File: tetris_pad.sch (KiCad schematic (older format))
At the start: 35 parts, among them P1 video, P2 ICSP, Q1 2N7000, SW1 ~reset, SW2 A, SW3 B, SW4 power, SW5 LEFT, SW6 UP, SW7 DOWN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

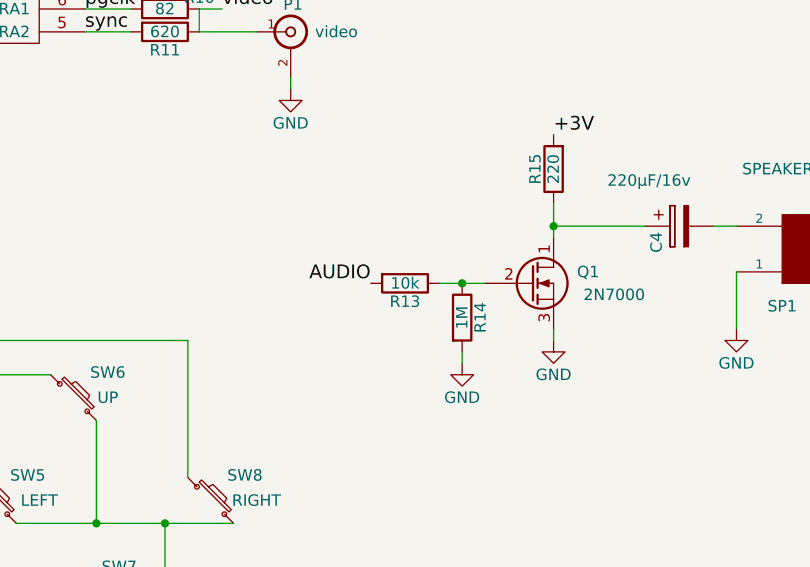
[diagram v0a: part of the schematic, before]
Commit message: schematic rework
renamed project tetris_pad
rework: read_pad, isr, xor_row
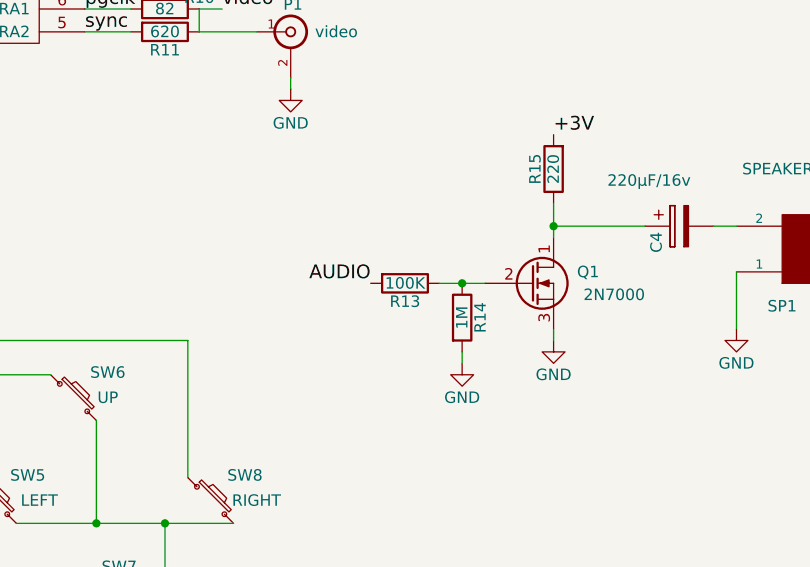
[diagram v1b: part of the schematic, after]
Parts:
- R13: value 10k -> 100K
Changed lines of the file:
@@
 LIBS:valves
 LIBS:Personal_KiCAD
-LIBS:ntsc_test-cache
+LIBS:tetris_pad-cache
 EELAYER 25 0
 EELAYER END
@@
 Wire Wire Line
 	7800 4200 8000 4200
-$Comp
-L R R13
-U 1 1 584C5448
-P 7650 4200
-F 0 "R13" V 7730 4200 50  0000 C CNN
-F 1 "10k" V 7650 4200 50  0000 C CNN
-F 2 "" V 7580 4200 50  0000 C CNN
-F 3 "" H 7650 4200 50  0000 C CNN
-	1    7650 4200
-	0    1    1    0
-$EndComp
 Connection ~ 7900 4200
 Text Label 7500 4200 2    60   ~ 0
@@
 Wire Wire Line
 	4050 4050 3500 4050
+$Comp
+L R R13
+U 1 1 584D7E45
+P 7650 4200
+F 0 "R13" V 7730 4200 50  0000 C CNN
+F 1 "100K" V 7650 4200 50  0000 C CNN
+F 2 "" V 7580 4200 50  0000 C CNN
+F 3 "" H 7650 4200 50  0000 C CNN
+	1    7650 4200
+	0    1    1    0
+$EndComp
 $EndSCHEMATC

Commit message: further optimization
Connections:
- net AUDIO: no longer R3.1, R4.2, R5.1, U1.3 (RA4)
- new net AUDIO/BTN: R3.1, R4.2, R5.1, U1.3 (RA4)
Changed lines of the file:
@@
 AUDIO
 Text Label 5350 3000 2    39   ~ 0
-AUDIO
+AUDIO/BTN
 Wire Wire Line
 	4350 4050 4900 4050

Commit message: finalization
reordering tasks in isr
removed get_next_word from get_nibble, was never called.
actual size: 1031i
My optimization efforts will end here. I can't expect gaining
more than a few instructions.
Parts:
- BT1: value 2xAAA -> CR2450
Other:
- note added: "optional"
- moved on the sheet: C4, Q1, R13, R14, R15, SP1
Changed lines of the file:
@@
 P 4600 2250
 F 0 "BT1" H 4700 2300 50  0000 L CNN
-F 1 "2xAAA" H 4700 2200 50  0000 L CNN
+F 1 "CR2450" H 4700 2200 50  0000 L CNN
 F 2 "" V 4600 2290 50  0000 C CNN
 F 3 "" V 4600 2290 50  0000 C CNN
@@
 L SPEAKER SP1
 U 1 1 58432B86
-P 9400 4050
-F 0 "SP1" H 9300 4300 50  0000 C CNN
-F 1 "SPEAKER 8 ohm" H 9400 3700 50  0000 C CNN
-F 2 "" H 9400 4050 50  0000 C CNN
-F 3 "" H 9400 4050 50  0000 C CNN
-	1    9400 4050
+P 9450 4350
+F 0 "SP1" H 9350 4600 50  0000 C CNN
+F 1 "SPEAKER 8 ohm" H 9450 4000 50  0000 C CNN
+F 2 "" H 9450 4350 50  0000 C CNN
+F 3 "" H 9450 4350 50  0000 C CNN
+	1    9450 4350
 	1    0    0    1
 $EndComp
@@
 L GND #PWR10
 U 1 1 58432BE5
-P 9100 4400
-F 0 "#PWR10" H 9100 4150 50  0001 C CNN
-F 1 "GND" H 9100 4250 50  0000 C CNN
-F 2 "" H 9100 4400 50  0000 C CNN
-F 3 "" H 9100 4400 50  0000 C CNN
-	1    9100 4400
+P 9150 4700
+F 0 "#PWR10" H 9150 4450 50  0001 C CNN
+F 1 "GND" H 9150 4550 50  0000 C CNN
+F 2 "" H 9150 4700 50  0000 C CNN
+F 3 "" H 9150 4700 50  0000 C CNN
+	1    9150 4700
 	-1   0    0    -1
 $EndComp
@@
 L CP C4
 U 1 1 58432C79
-P 8850 3950
-F 0 "C4" H 8875 4050 50  0000 L CNN
-F 1 "220µF/16v" V 8650 3900 50  0000 L CNN
-F 2 "" H 8888 3800 50  0000 C CNN
-F 3 "" H 8850 3950 50  0000 C CNN
-	1    8850 3950
+P 8900 4250
+F 0 "C4" H 8925 4350 50  0000 L CNN
+F 1 "220µF/16v" V 8700 4200 50  0000 L CNN
+F 2 "" H 8938 4100 50  0000 C CNN
+F 3 "" H 8900 4250 50  0000 C CNN
+	1    8900 4250
 	0    -1   1    0
 $EndComp
@@
 	2650 2050 2650 2200
 Wire Wire Line
-	9100 4150 9100 4400
-Wire Wire Line
-	9100 3950 9000 3950
+	9150 4450 9150 4700
+Wire Wire Line
+	9150 4250 9050 4250
 Wire Wire Line
 	4600 5900 5150 5900
@@
 L R R15
 U 1 1 584B92CB
-P 8300 3700
-F 0 "R15" V 8380 3700 50  0000 C CNN
-F 1 "220" V 8300 3700 50  0000 C CNN
-F 2 "" V 8230 3700 50  0000 C CNN
-F 3 "" H 8300 3700 50  0000 C CNN
-	1    8300 3700
+P 8350 4000
+F 0 "R15" V 8430 4000 50  0000 C CNN
+F 1 "220" V 8350 4000 50  0000 C CNN
+F 2 "" V 8280 4000 50  0000 C CNN
+F 3 "" H 8350 4000 50  0000 C CNN
+	1    8350 4000
 	-1   0    0    1
 $EndComp
 Wire Wire Line
-	8300 3950 8700 3950
+	8350 4250 8750 4250
 Wire Wire Line
 	6850 2900 6250 2900
@@
 L Q_NMOS_DGS Q1
 U 1 1 584C4D58
-P 8200 4200
-F 0 "Q1" H 8500 4250 50  0000 R CNN
-F 1 "2N7000" H 8700 4150 50  0000 R CNN
-F 2 "" H 8400 4300 50  0000 C CNN
-F 3 "" H 8200 4200 50  0000 C CNN
-	1    8200 4200
-	1    0    0    -1
-$EndComp
-Text Label 8300 3550 0    60   ~ 0
+P 8250 4500
+F 0 "Q1" H 8550 4550 50  0000 R CNN
+F 1 "2N7000" H 8750 4450 50  0000 R CNN
+F 2 "" H 8450 4600 50  0000 C CNN
+F 3 "" H 8250 4500 50  0000 C CNN
+	1    8250 4500
+	1    0    0    -1
+$EndComp
+Text Label 8350 3850 0    60   ~ 0
 +3V
 Wire Wire Line
-	8300 3850 8300 4000
-Connection ~ 8300 3950
+	8350 4150 8350 4300
+Connection ~ 8350 4250
 $Comp
 L GND #PWR9
 U 1 1 584C5093
-P 8300 4450
-F 0 "#PWR9" H 8300 4200 50  0001 C CNN
-F 1 "GND" H 8300 4300 50  0000 C CNN
-F 2 "" H 8300 4450 50  0000 C CNN
-F 3 "" H 8300 4450 50  0000 C CNN
-	1    8300 4450
+P 8350 4750
+F 0 "#PWR9" H 8350 4500 50  0001 C CNN
+F 1 "GND" H 8350 4600 50  0000 C CNN
+F 2 "" H 8350 4750 50  0000 C CNN
+F 3 "" H 8350 4750 50  0000 C CNN
+	1    8350 4750
 	-1   0    0    -1
 $EndComp
 Wire Wire Line
-	8300 4400 8300 4450
+	8350 4700 8350 4750
 $Comp
 L R R14
 U 1 1 584C5206
-P 7900 4350
-F 0 "R14" V 7980 4350 50  0000 C CNN
-F 1 "1M" V 7900 4350 50  0000 C CNN
-F 2 "" V 7830 4350 50  0000 C CNN
-F 3 "" H 7900 4350 50  0000 C CNN
-	1    7900 4350
+P 7950 4650
+F 0 "R14" V 8030 4650 50  0000 C CNN
+F 1 "1M" V 7950 4650 50  0000 C CNN
+F 2 "" V 7880 4650 50  0000 C CNN
+F 3 "" H 7950 4650 50  0000 C CNN
+	1    7950 4650
 	1    0    0    -1
 $EndComp
@@
 L GND #PWR8
 U 1 1 584C531A
-P 7900 4550
-F 0 "#PWR8" H 7900 4300 50  0001 C CNN
-F 1 "GND" H 7900 4400 50  0000 C CNN
-F 2 "" H 7900 4550 50  0000 C CNN
-F 3 "" H 7900 4550 50  0000 C CNN
-	1    7900 4550
+P 7950 4850
+F 0 "#PWR8" H 7950 4600 50  0001 C CNN
+F 1 "GND" H 7950 4700 50  0000 C CNN
+F 2 "" H 7950 4850 50  0000 C CNN
+F 3 "" H 7950 4850 50  0000 C CNN
+	1    7950 4850
 	-1   0    0    -1
 $EndComp
 Wire Wire Line
-	7900 4500 7900 4550
-Wire Wire Line
-	7800 4200 8000 4200
-Connection ~ 7900 4200
-Text Label 7500 4200 2    60   ~ 0
+	7950 4800 7950 4850
+Wire Wire Line
+	7850 4500 8050 4500
+Connection ~ 7950 4500
+Text Label 7550 4500 2    60   ~ 0
 AUDIO
 Text Label 5350 3000 2    39   ~ 0
@@
 L R R13
 U 1 1 584D7E45
-P 7650 4200
-F 0 "R13" V 7730 4200 50  0000 C CNN
-F 1 "100K" V 7650 4200 50  0000 C CNN
-F 2 "" V 7580 4200 50  0000 C CNN
-F 3 "" H 7650 4200 50  0000 C CNN
-	1    7650 4200
+P 7700 4500
+F 0 "R13" V 7780 4500 50  0000 C CNN
+F 1 "100K" V 7700 4500 50  0000 C CNN
+F 2 "" V 7630 4500 50  0000 C CNN
+F 3 "" H 7700 4500 50  0000 C CNN
+	1    7700 4500
 	0    1    1    0
 $EndComp
+Wire Notes Line
+	7250 3700 7250 5200
+Wire Notes Line
+	7250 5200 9800 5200
+Wire Notes Line
+	9800 5200 9800 3700
+Wire Notes Line
+	9800 3700 7250 3700
+Text Notes 7400 3850 0    60   ~ 0
+optional
 $EndSCHEMATC

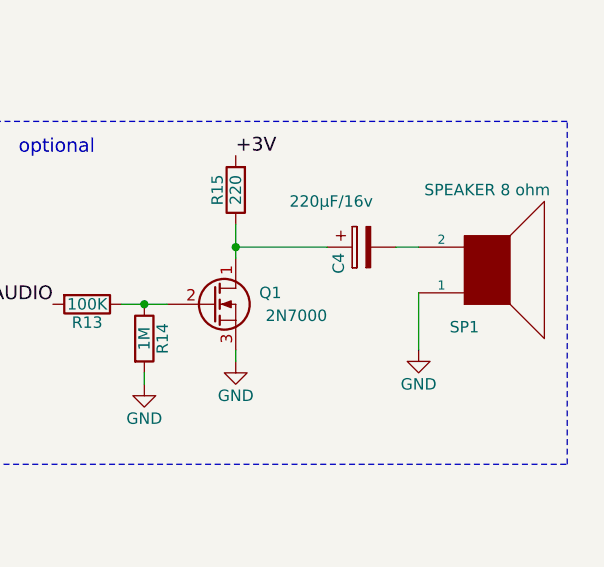
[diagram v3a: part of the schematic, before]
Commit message: modified hardware audio circuit.
audio level to low circuit modified for an output to TV.
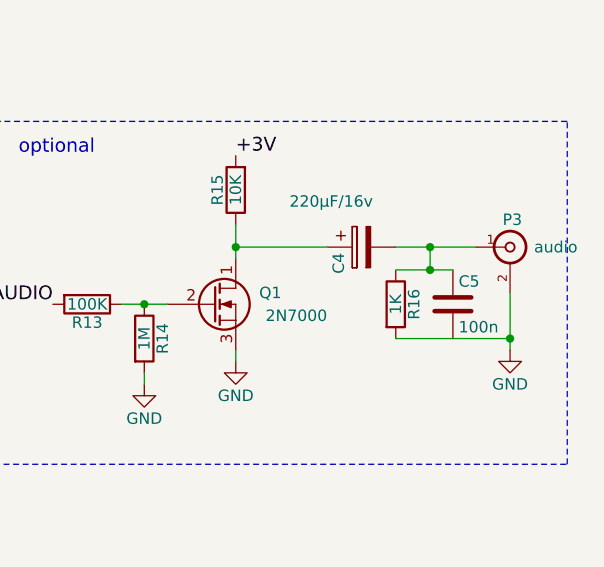
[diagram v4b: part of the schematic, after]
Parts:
- removed SP1: SPEAKER 8 ohm, symbol SPEAKER
- added C5: 100n, symbol C
- added P3: audio, symbol BNC
- added R16: 1K, symbol R
- R15: value 220 -> 10K
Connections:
- net GND: now also P3.2 (Ext), R16.2
- net at C4.2: now also C5.1, P3.1 (In), R16.1
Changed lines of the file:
@@
 Vpp/~rst
-$Comp
-L SPEAKER SP1
-U 1 1 58432B86
-P 9450 4350
-F 0 "SP1" H 9350 4600 50  0000 C CNN
-F 1 "SPEAKER 8 ohm" H 9450 4000 50  0000 C CNN
-F 2 "" H 9450 4350 50  0000 C CNN
-F 3 "" H 9450 4350 50  0000 C CNN
-	1    9450 4350
-	1    0    0    1
-$EndComp
 $Comp
 L GND #PWR10
 U 1 1 58432BE5
-P 9150 4700
-F 0 "#PWR10" H 9150 4450 50  0001 C CNN
-F 1 "GND" H 9150 4550 50  0000 C CNN
-F 2 "" H 9150 4700 50  0000 C CNN
-F 3 "" H 9150 4700 50  0000 C CNN
-	1    9150 4700
+P 9550 4700
+F 0 "#PWR10" H 9550 4450 50  0001 C CNN
+F 1 "GND" H 9550 4550 50  0000 C CNN
+F 2 "" H 9550 4700 50  0000 C CNN
+F 3 "" H 9550 4700 50  0000 C CNN
+	1    9550 4700
 	-1   0    0    -1
 $EndComp
@@
 	2650 2050 2650 2200
 Wire Wire Line
-	9150 4450 9150 4700
-Wire Wire Line
-	9150 4250 9050 4250
+	9550 4450 9550 4700
+Wire Wire Line
+	9050 4250 9400 4250
 Wire Wire Line
 	4600 5900 5150 5900
@@
 P 8350 4000
 F 0 "R15" V 8430 4000 50  0000 C CNN
-F 1 "220" V 8350 4000 50  0000 C CNN
+F 1 "10K" V 8350 4000 50  0000 C CNN
 F 2 "" V 8280 4000 50  0000 C CNN
 F 3 "" H 8350 4000 50  0000 C CNN
@@
 Text Notes 7400 3850 0    60   ~ 0
 optional
+$Comp
+L BNC P3
+U 1 1 585AA9B3
+P 9550 4250
+F 0 "P3" H 9560 4370 50  0000 C CNN
+F 1 "audio" H 9750 4250 50  0000 C CNN
+F 2 "" H 9550 4250 50  0000 C CNN
+F 3 "" H 9550 4250 50  0000 C CNN
+	1    9550 4250
+	1    0    0    -1
+$EndComp
+$Comp
+L R R16
+U 1 1 585AAAE6
+P 9050 4500
+F 0 "R16" V 9130 4500 50  0000 C CNN
+F 1 "1K" V 9050 4500 50  0000 C CNN
+F 2 "" V 8980 4500 50  0000 C CNN
+F 3 "" H 9050 4500 50  0000 C CNN
+	1    9050 4500
+	1    0    0    -1
+$EndComp
+$Comp
+L C C5
+U 1 1 585AAB81
+P 9300 4500
+F 0 "C5" H 9325 4600 50  0000 L CNN
+F 1 "100n" H 9325 4400 50  0000 L CNN
+F 2 "" H 9338 4350 50  0000 C CNN
+F 3 "" H 9300 4500 50  0000 C CNN
+	1    9300 4500
+	1    0    0    -1
+$EndComp
+Wire Wire Line
+	9050 4650 9550 4650
+Connection ~ 9550 4650
+Wire Wire Line
+	9050 4350 9300 4350
+Wire Wire Line
+	9200 4350 9200 4250
+Connection ~ 9200 4250
+Connection ~ 9200 4350
 $EndSCHEMATC
